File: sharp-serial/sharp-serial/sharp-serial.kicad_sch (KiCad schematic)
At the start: 2 parts, among them J1 sharp_connector_15pin, U1 FT232RL_breakout

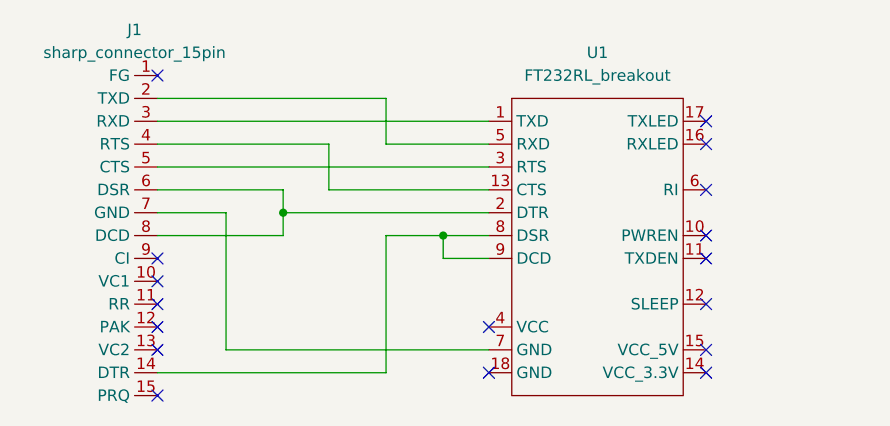
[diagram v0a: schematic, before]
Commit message: USB->serial connector for Sharp using 6pins FT232RL cable
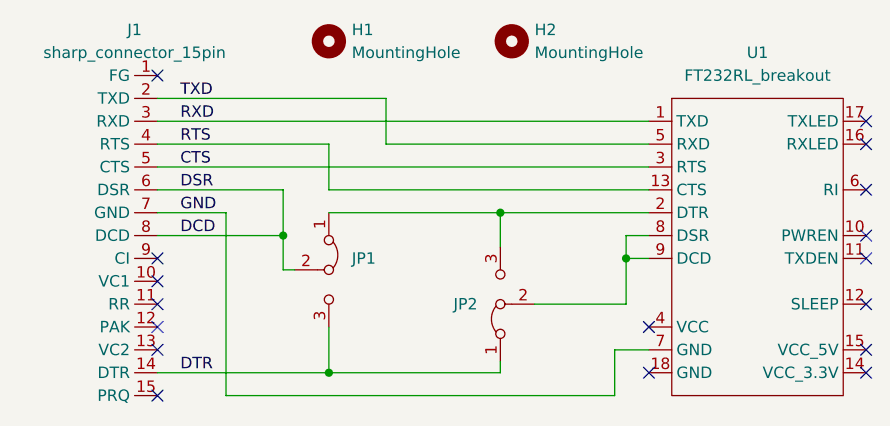
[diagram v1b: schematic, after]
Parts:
- added H1, H2: MountingHole, MountingHole:MountingHole_2.5mm, symbol Mechanical:MountingHole
- added JP1, JP2: Jumper_3_Bridged12, Connector_PinHeader_2.54mm:PinHeader_1x03_P2.54mm_Vertical, symbol Jumper:Jumper_3_Bridged12
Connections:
- net RXD: now reaches J1.3 (RXD), U1.1 (TXD)
- net RTS: now reaches J1.4 (RTS), U1.13 (CTS)
- net DCD: now reaches J1.6 (DSR), J1.8 (DCD)
- net DCD: now also JP1.2 (C); no longer U1.2 (DTR)
- net CTS: now reaches J1.5 (CTS), U1.3 (RTS)
- net TXD: now reaches J1.2 (TXD), U1.5 (RXD)
- net GND: now reaches J1.7 (GND), U1.7 (GND)
- net at U1.8 (DSR), U1.9 (DCD): now also JP2.2 (C); no longer J1.14 (DTR)
- new net: JP1.1 (A), JP2.3 (B), U1.2 (DTR)
- new net DTR: J1.14 (DTR), JP1.3 (B), JP2.1 (A)
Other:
- moved on the sheet: U1
